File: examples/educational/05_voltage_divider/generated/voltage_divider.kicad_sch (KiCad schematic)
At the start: 3 parts

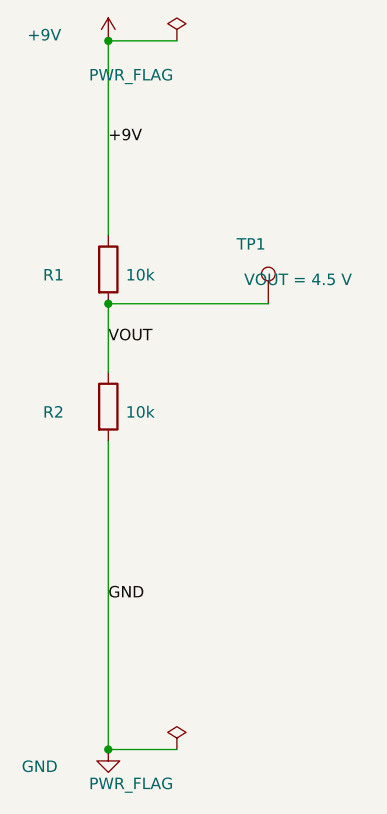
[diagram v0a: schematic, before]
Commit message: feat: infer conventional schematic topology layouts
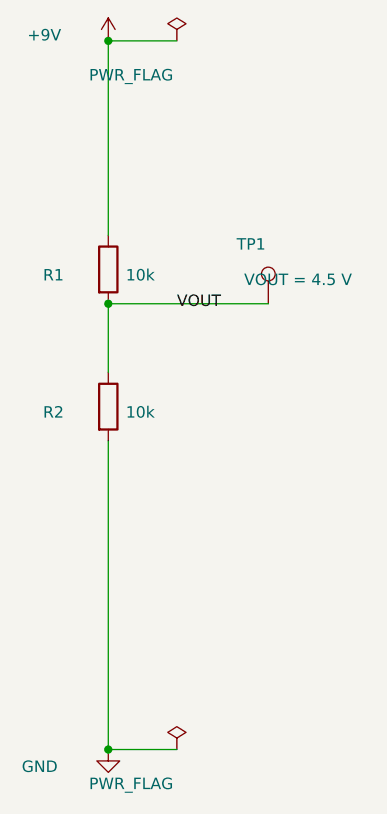
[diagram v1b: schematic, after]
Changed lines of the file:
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@@
   (wire
     (pts
+      (xy 111.76 138.43)
       (xy 93.98 138.43)
-      (xy 111.76 138.43)
-    )
-    (stroke
-      (width 0)
-      (type default)
-    )
-  )
-  (wire
-    (pts
-      (xy 93.98 146.05)
-      (xy 93.98 138.43)
-    )
-    (stroke
-      (width 0)
-      (type default)
-    )
-  )
-  (wire
-    (pts
-      (xy 93.98 187.96)
-      (xy 93.98 153.67)
     )
     (stroke
@@
   (wire
     (pts
+      (xy 93.98 153.67)
+      (xy 93.98 187.96)
+    )
+    (stroke
+      (width 0)
+      (type default)
+    )
+  )
+  (wire
+    (pts
+      (xy 93.98 130.81)
+      (xy 93.98 109.22)
+    )
+    (stroke
+      (width 0)
+      (type default)
+    )
+  )
+  (wire
+    (pts
       (xy 93.98 187.96)
       (xy 101.6 187.96)
@@
   (wire
     (pts
-      (xy 93.98 109.22)
-      (xy 93.98 130.81)
+      (xy 93.98 138.43)
+      (xy 93.98 146.05)
     )
     (stroke
@@
   )
   (label
-    "GND"
-    (at 93.98 170.815 0)
+    "VOUT"
+    (at 101.6 138.43 0)
     (effects
       (font
-        (size 1.27 1.27)
-      )
-    )
-  )
-  (label
-    "+9V"
-    (at 93.98 120.015 0)
-    (effects
-      (font
-        (size 1.27 1.27)
-      )
-    )
-  )
-  (label
-    "VOUT"
-    (at 93.98 142.24 0)
-    (effects
-      (font
